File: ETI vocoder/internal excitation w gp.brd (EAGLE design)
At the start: 114.9 x 38.4 mm, 51 parts, among them IC1 LM1458N, IC3 TL081P, IC4 UA741P, IC5 4006N, IC6 4030N, IC7 LM1458N, Q1 BC182L

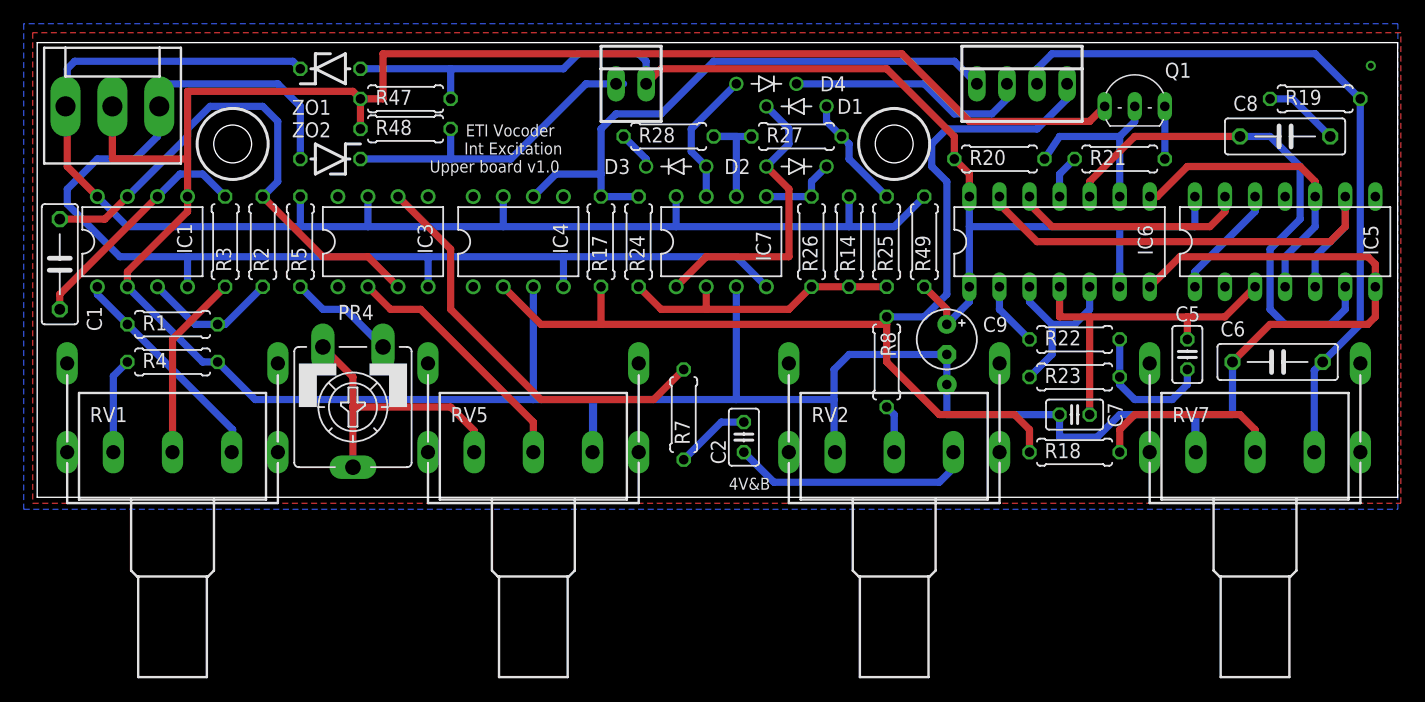
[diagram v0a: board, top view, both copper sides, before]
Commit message: Updated trimpot names and positions
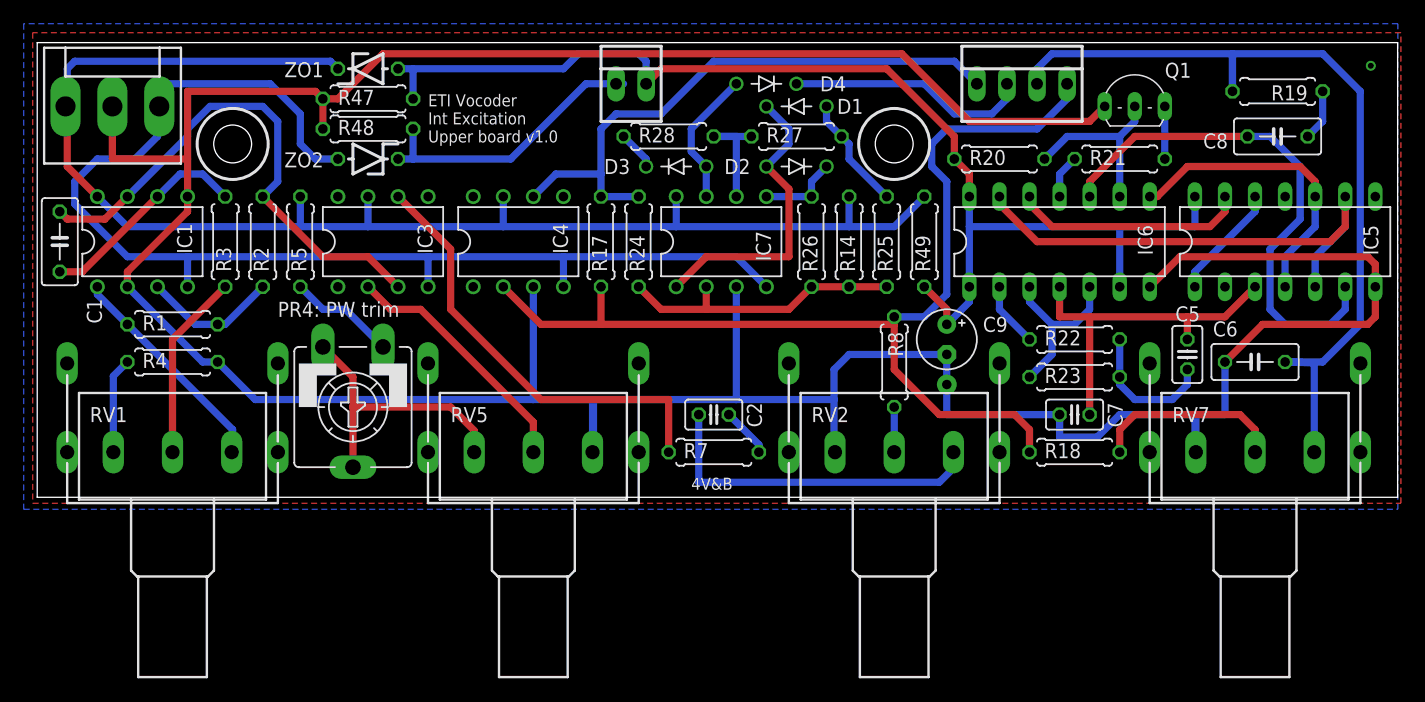
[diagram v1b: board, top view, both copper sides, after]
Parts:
- C1, C6, C8: device resistor:C075-032X103 -> resistor:C050-030X075
- moved R7 4.07 mm to (57.1, 3.81), turned to 180 degrees
- moved R19 3.24 mm to (104.8, 34.3), turned to 0 degrees
- moved ZO1 3.18 mm to (27.9, 36.2)
- moved ZO2 3.18 mm to (27.9, 28.6)
- moved C2 3.17 mm to (57.1, 6.99), turned to 0 degrees
- moved R47 3.17 mm to (27.9, 33.7)
- moved R48 3.17 mm to (27.9, 31.1)
- moved C1 1.91 mm to (1.91, 21.6)
- moved C6 1.91 mm to (102.9, 11.4)
- moved R8 0.64 mm to (72.4, 11.4)
- moved C8 0.63 mm to (104.8, 30.5)
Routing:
- net VCA_SIGNAL: track 62.1 -> 74.1 mm
- net N$12: track 20.6 -> 29.1 mm
- net VDD: track 106.1 -> 102.9 mm
- net VSS: track 27.4 -> 24.2 mm
- net +12V: track 117.0 -> 120.2 mm
- net GND: track 305.6 -> 303.4 mm
- net N$11: track 6.40 -> 4.23 mm
- net N$10: track 35.3 -> 37.4 mm
- net N$4: track 20.2 -> 18.2 mm
- net N$25: track 6.40 -> 4.34 mm
- net -12V: track 102.3 -> 103.4 mm
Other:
- board text added: "PR4: PW trim"
